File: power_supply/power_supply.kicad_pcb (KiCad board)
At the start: 2 copper layers, 100 x 90 mm, 49 parts, among them J2 Alimentação AC, J3 SAÍDA, Q1 TIP122, T1 35VAC - 3A, U1 CA3140, U2 ICL7107CPL, U3 ICL7660, U4 LM7824_TO220, U5 LM7805_TO220

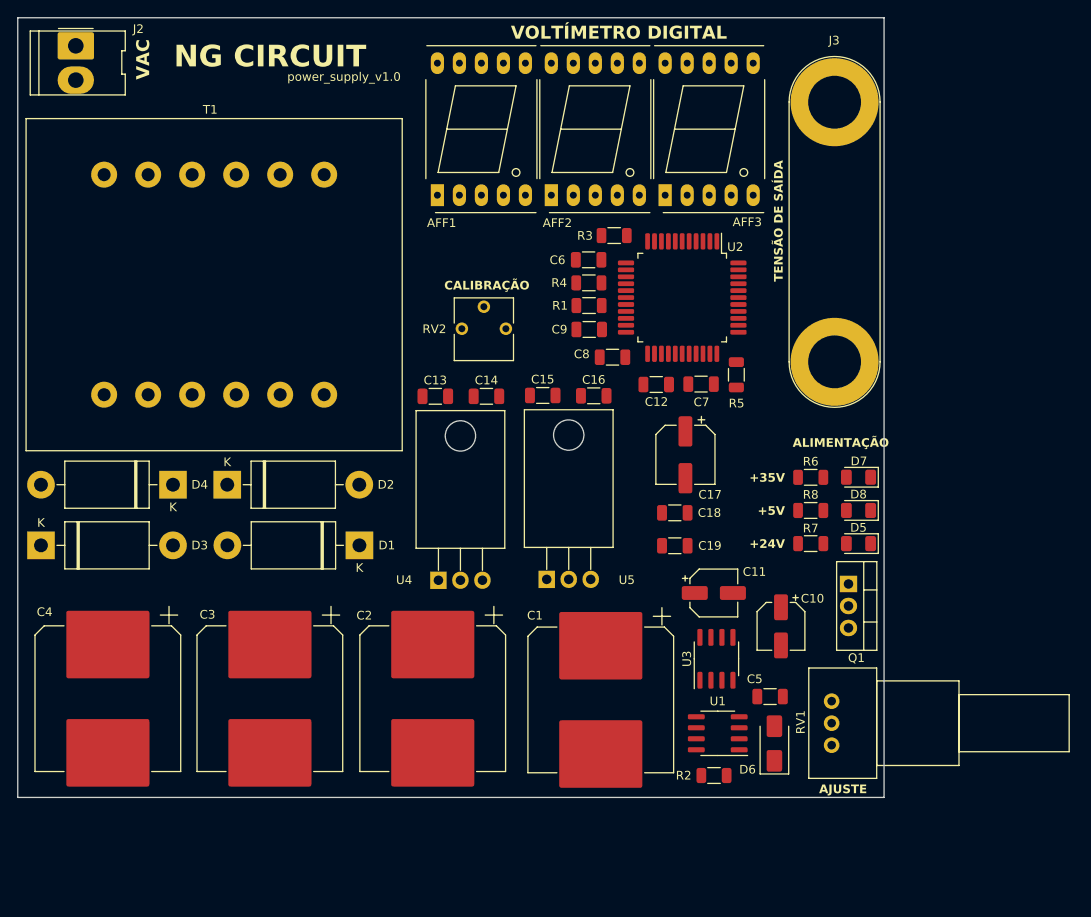
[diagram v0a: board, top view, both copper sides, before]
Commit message: Retira do Transformador On-Board para externo, troca de footprint para um conector Molex de 4 vias (3.96mm); Início do roteamento das trilhas e isolação dos planos GND.
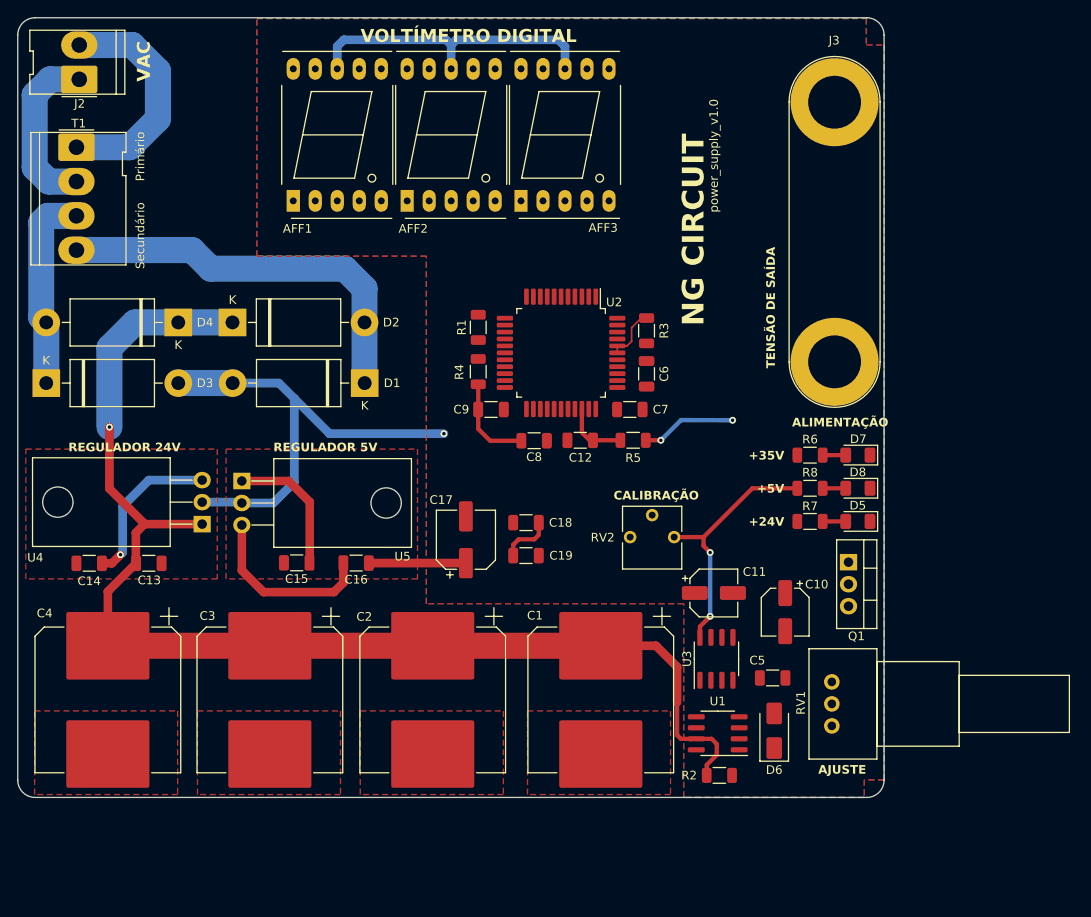
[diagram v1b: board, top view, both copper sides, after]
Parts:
- T1: footprint Transformer_THT:Transformer_37x44 -> Connector_Molex:Molex_KK-396_5273-04A_1x04_P3.96mm_Vertical
- moved C14 49.7 mm to (98.2, 111.0), turned to 180 degrees
- moved C13 38.3 mm to (105.1, 111.0)
- moved U5 37.0 mm to (115.9, 101.5), turned to -90 degrees
- moved C15 34.4 mm to (122.2, 110.9), turned to 180 degrees
- moved C16 33.5 mm to (129.1, 110.9)
- moved RV2 30.9 mm to (165.8, 108.0)
- moved U4 28.0 mm to (111.3, 106.5), turned to 90 degrees
- moved C17 27.2 mm to (141.7, 108.3), turned to 90 degrees
- moved D1 18.7 mm to (130.0, 90.2)
- moved D4 18.7 mm to (108.5, 83.2)
- moved D2 18.7 mm to (114.8, 83.2)
- moved D3 18.7 mm to (93.3, 90.2)
- moved C18 17.2 mm to (148.7, 106.3)
- moved C19 17.2 mm to (148.7, 110.1)
- moved AFF2 16.7 mm to (135.0, 69.1)
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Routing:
- net VDC: track 0.00 -> 143.6 mm, vias 0 -> 1
- net +5V: track 0.00 -> 85.0 mm, vias 0 -> 2
- net GNDREF: track 0.00 -> 54.4 mm, vias 0 -> 1
- net Net-(D1-K): track 0.00 -> 46.0 mm
- net VAC1: track 0.00 -> 26.6 mm
- net Net-(D3-K): track 0.00 -> 23.2 mm
- net VAC2: track 0.00 -> 19.8 mm
- net +24V: track 0.00 -> 18.7 mm, vias 0 -> 1
- net 24V: track 0.00 -> 15.9 mm
- net Net-(C16-Pad2): track 0.00 -> 11.2 mm
- net Vout: track 0.00 -> 11.1 mm, vias 0 -> 2
- net Net-(C8-Pad1): track 0.00 -> 10.7 mm
- net Net-(U2-IN_HI): track 0.00 -> 7.54 mm
- net Net-(U2-OSC1): track 0.00 -> 6.44 mm
- net Net-(C18-Pad2): track 0.00 -> 6.08 mm
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- added copper zone on B.Cu, net GNDREF
- added copper zone on F.Cu, net GNDREF
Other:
- outline, holes or cut-outs redrawn
- board text added: "Primário"
- board text added: "REGULADOR 24V"
- board text added: "REGULADOR 5V"
- board text added: "Secundário"

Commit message: Finalização do Layout, aguardando dúvida das Vias para trilhas de 3mm.
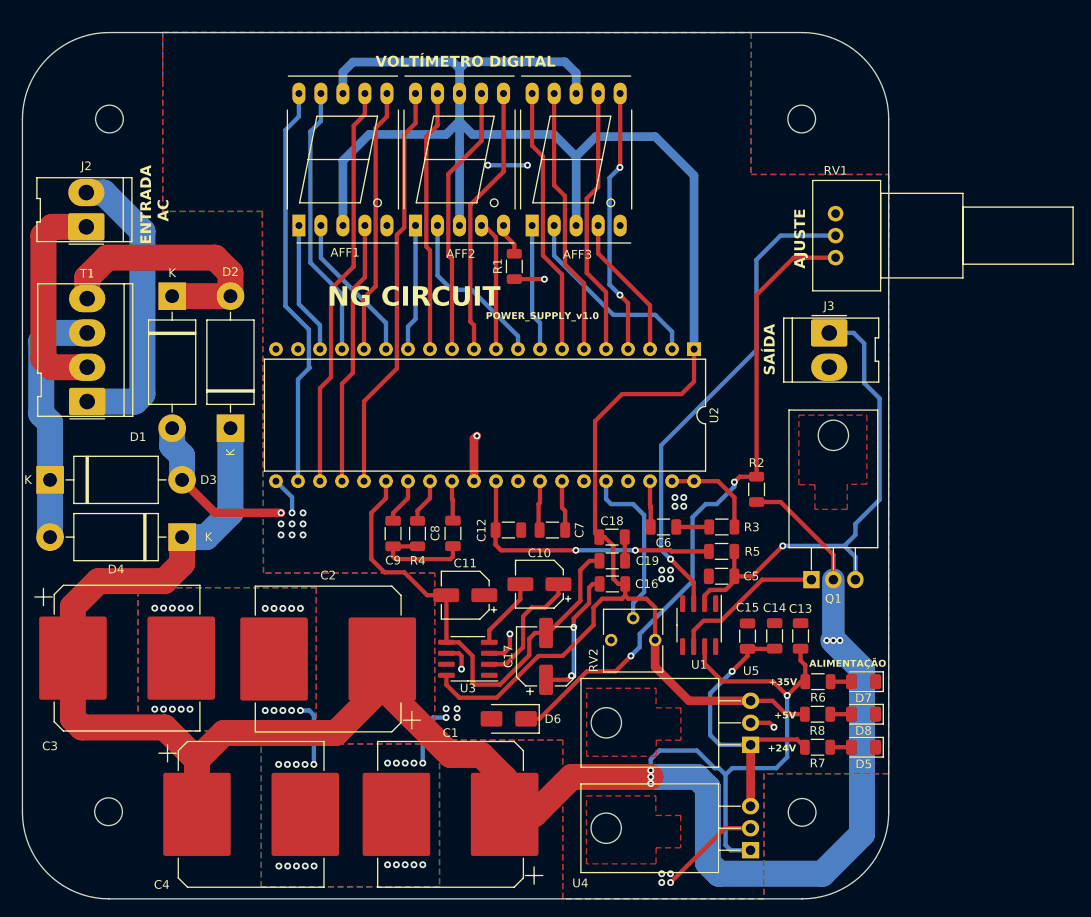
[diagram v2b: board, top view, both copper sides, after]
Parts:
- added H1: MountingHole, MountingHole:MountingHole_3.2mm_M3, F.Cu at (100.6, 59.7)
- added H2: MountingHole, MountingHole:MountingHole_3.2mm_M3, F.Cu at (180.5, 59.7)
- added H3: MountingHole, MountingHole:MountingHole_3.2mm_M3, F.Cu at (100.5, 139.6)
- added H4: MountingHole, MountingHole:MountingHole_3.2mm_M3, F.Cu at (180.5, 139.7)
- J3: footprint Connector:Banana_Jack_2Pin -> Connector_Molex:Molex_KK-396_5273-02A_1x02_P3.96mm_Vertical
- Q1: footprint Package_TO_SOT_THT:TO-220-3_Vertical -> Package_TO_SOT_THT:TO-220-3_Horizontal_TabDown
- U2: footprint Package_QFP:MQFP-44_10x10mm_P0.8mm -> Package_DIP:DIP-40_W15.24mm
- moved C14 79.6 mm to (177.4, 119.4), turned to 90 degrees
- moved C13 75.7 mm to (180.4, 119.4), turned to 90 degrees
- moved U4 73.6 mm to (174.6, 144.1)
- moved U5 66.2 mm to (174.6, 131.9), turned to 90 degrees
- moved RV1 54.1 mm to (184.4, 75.7)
- moved C15 52.7 mm to (174.2, 119.4), turned to 90 degrees
- moved R2 33.3 mm to (175.3, 102.4), turned to 90 degrees
- moved D6 30.7 mm to (146.7, 128.9), turned to 180 degrees
- moved C16 29.7 mm to (158.6, 113.4), turned to 180 degrees
- moved T1 29.4 mm to (98.0, 92.3), turned to 90 degrees
- moved C11 28.7 mm to (141.7, 114.7), turned to 180 degrees
- moved U3 28.7 mm to (142.0, 122.0), turned to 180 degrees
- moved C10 28.6 mm to (150.2, 113.4), turned to 180 degrees
- moved D7 26.2 mm to (187.6, 124.6)
- moved R6 26.2 mm to (182.4, 124.6)
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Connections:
- C15 pad 1: 24V -> +24V
- U5 pad 1: 24V -> +24V
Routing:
- net +5V: track 85.0 -> 232.3 mm, vias 2 -> 0
- net VDC: track 143.6 -> 281.2 mm, vias 1 -> 7
- net Net-(D6-K): track 0.00 -> 75.6 mm, vias 0 -> 2
- net Net-(U1-+): track 0.00 -> 56.1 mm, vias 0 -> 1
- net -5V: track 0.00 -> 56.1 mm
- net G2: track 0.00 -> 47.2 mm
- net G3: track 0.00 -> 47.1 mm
- net A3: track 0.00 -> 46.9 mm
- net Vout: track 11.1 -> 57.4 mm, vias 2 -> 1
- net F3: track 0.00 -> 31.5 mm
- net A2: track 0.00 -> 31.3 mm
- net B2: track 0.00 -> 31.3 mm
- net A1: track 0.00 -> 31.0 mm
- net F1: track 0.00 -> 30.9 mm
- net G1: track 0.00 -> 30.9 mm
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- added copper zone on F.Cu, net (none)
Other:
- board size 100 x 90 mm -> 100 x 100 mm
- board text added: "AC"
- board text added: "ENTRADA"
- board text added: "POWER_SUPPLY_v1.0"
- board text added: "SAÍDA"
- board text removed: "CALIBRAÇÃO"
- board text removed: "Primário"
- board text removed: "REGULADOR 24V"
- board text removed: "REGULADOR 5V"
- board text removed: "Secundário"
- board text removed: "TENSÃO DE SAÍDA"
- board text removed: "VAC"
- board text removed: "power_supply_v1.0"

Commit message: Finalização/Correção do Layout solicitado!
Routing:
- net GNDREF: track 74.5 -> 50.8 mm, vias 72 -> 27

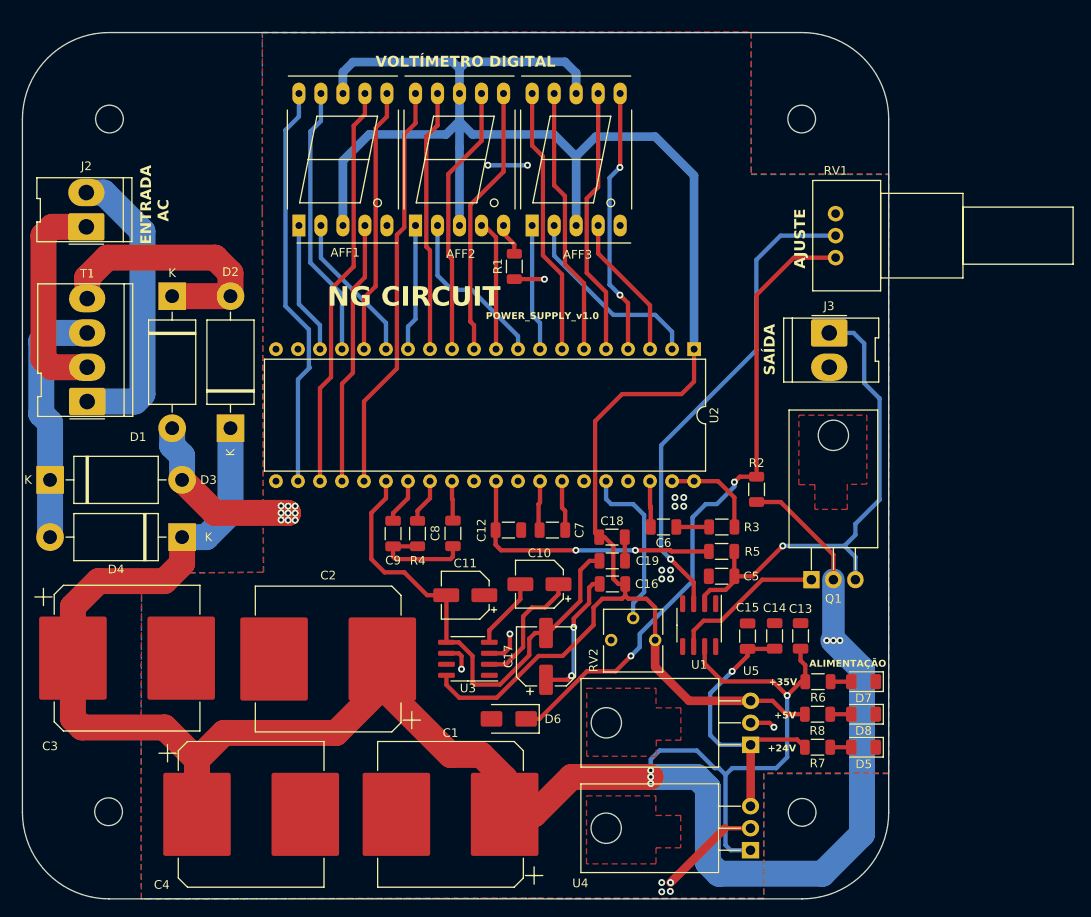
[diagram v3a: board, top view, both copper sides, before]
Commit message: Atualização de Trilhas e adicionado fotos do 3D atualizado
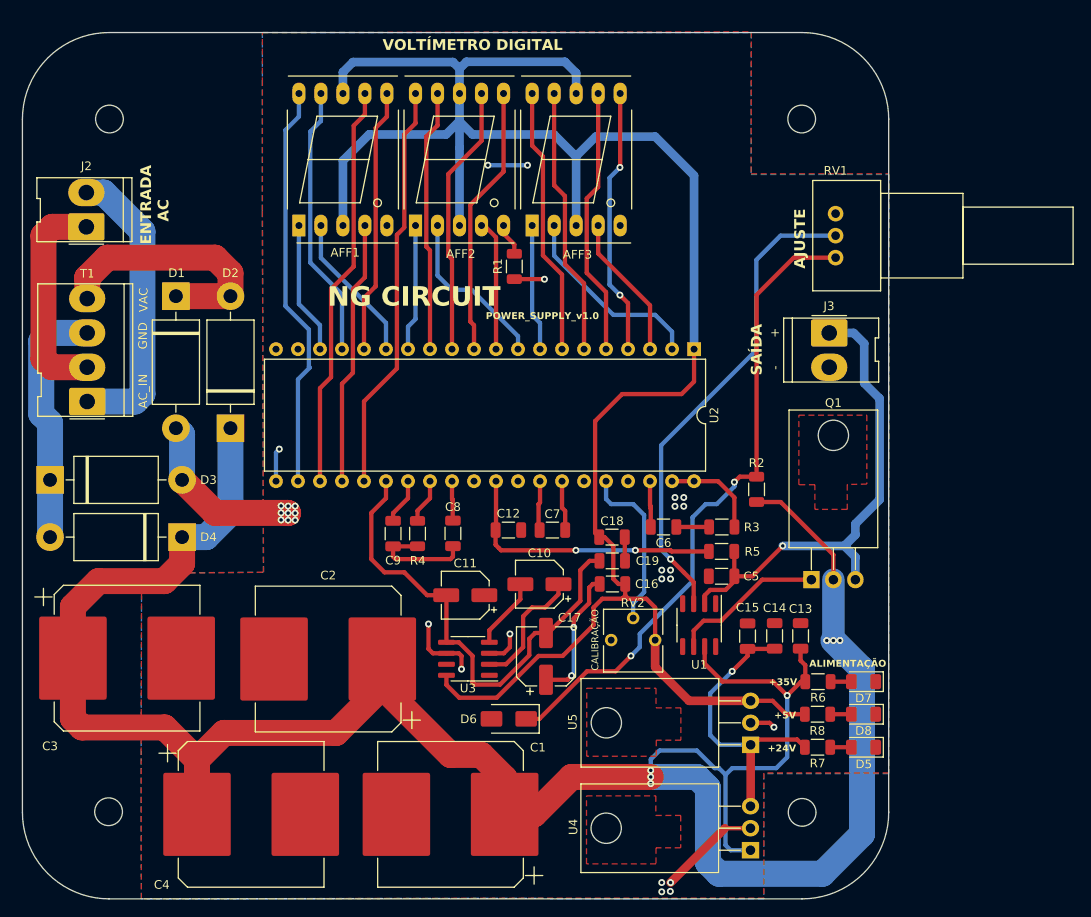
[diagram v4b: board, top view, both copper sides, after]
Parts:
- moved D1 0.43 mm to (108.3, 80.1)
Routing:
- net GNDREF: track 50.8 -> 59.7 mm, vias 27 -> 29
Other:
- board text added: "+"
- board text added: "-"
- board text added: "AC_IN"
- board text added: "CALIBRAÇÃO"
- board text added: "GND"
- board text added: "VAC"
